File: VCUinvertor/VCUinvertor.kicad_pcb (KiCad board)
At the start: 2 copper layers, 97.3 x 113.8 mm, 107 parts, among them J7 PowerSupply, J9 BRAKE LIGHT, Q1 2N7002, Q10 2N7002, Q11 BC848C, Q12 BCP51, Q2 2N7002, Q3 2N7002, Q4 2N7002, Q5 2N7002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

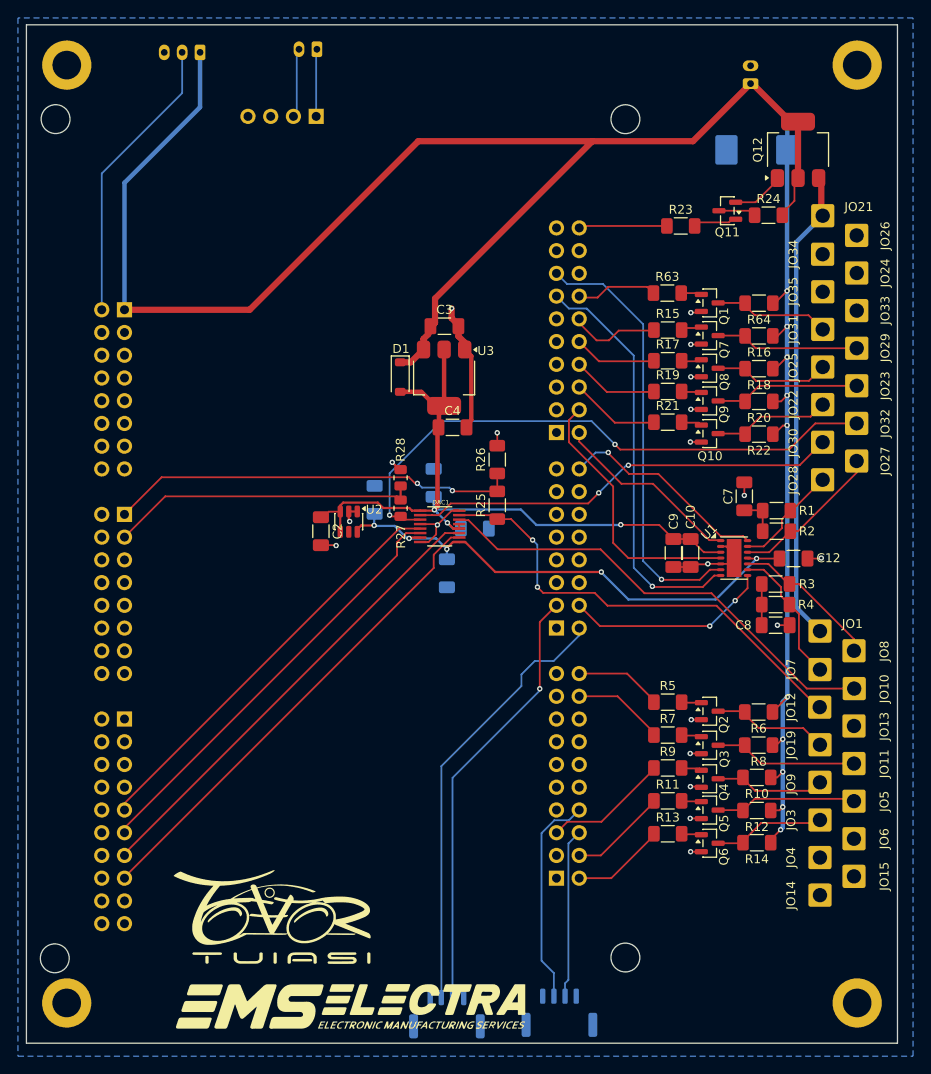
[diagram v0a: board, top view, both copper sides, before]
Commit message: TestPoints added
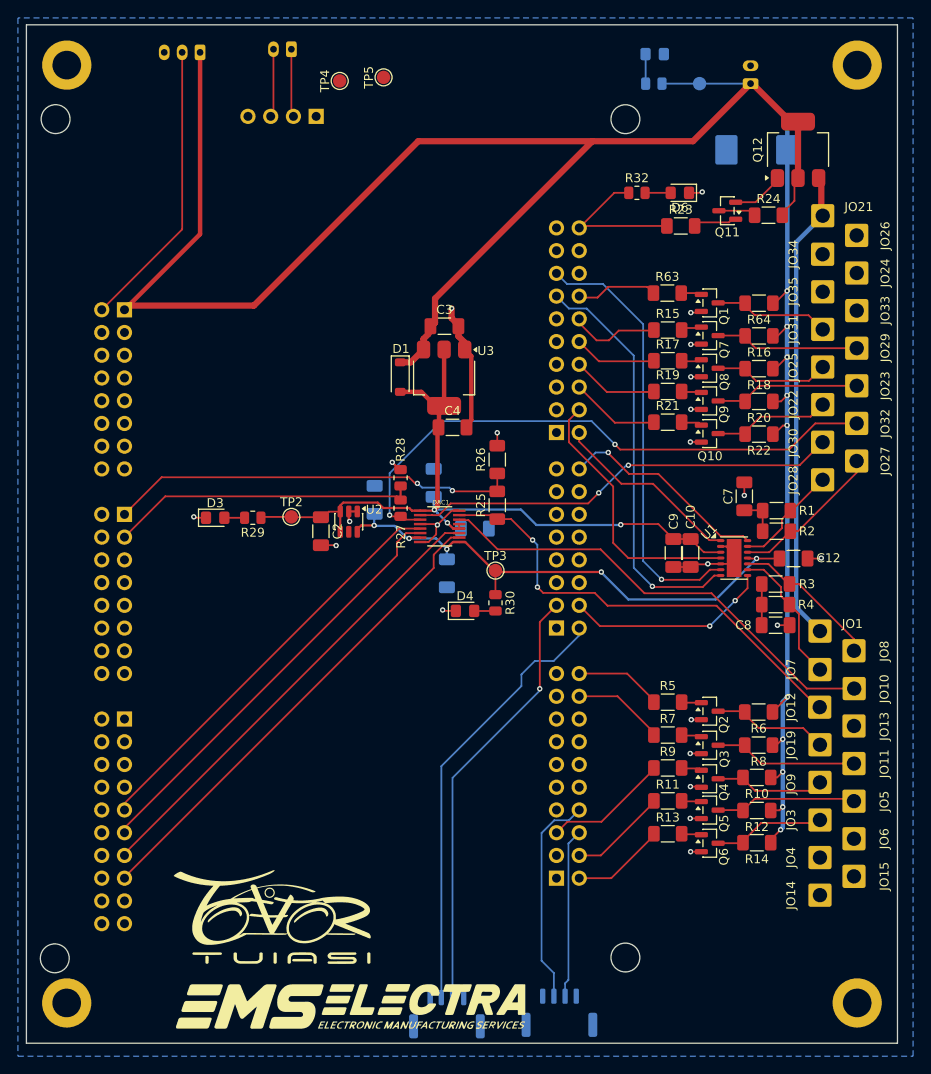
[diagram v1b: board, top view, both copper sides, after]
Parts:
- added 12V1: 12V, TestPoint:TestPoint_Pad_D1.5mm, B.Cu at (128.2, 44.3)
- added D3: LED, LED_SMD:LED_0805_2012Metric_Pad1.15x1.40mm_HandSolder, F.Cu at (74.0, 92.8)
- added D4: LED, LED_SMD:LED_0805_2012Metric_Pad1.15x1.40mm_HandSolder, F.Cu at (102.0, 103.2)
- added D5: LED, LED_SMD:LED_0805_2012Metric_Pad1.15x1.40mm_HandSolder, B.Cu at (123.1, 41.0)
- added D6: LED, LED_SMD:LED_0805_2012Metric_Pad1.15x1.40mm_HandSolder, F.Cu at (126.0, 56.5)
- added R29: 1k, Resistor_SMD:R_0805_2012Metric, F.Cu at (78.2, 92.8)
- added R30: 1k, Resistor_SMD:R_0805_2012Metric, F.Cu at (105.4, 102.3)
- added R31: 2.2k, Resistor_SMD:R_0805_2012Metric, B.Cu at (123.0, 44.3)
- added R32: 1k, Resistor_SMD:R_0805_2012Metric, F.Cu at (121.2, 56.5)
- added TP2: 5V, TestPoint:TestPoint_Pad_D1.5mm, F.Cu at (82.6, 92.7)
- added TP3: 3.3V, TestPoint:TestPoint_Pad_D1.5mm, F.Cu at (105.4, 98.7)
- added TP4: CANH, TestPoint:TestPoint_Pad_D1.5mm, F.Cu at (88.0, 44.0)
- added TP5: CANL, TestPoint:TestPoint_Pad_D1.5mm, F.Cu at (92.9, 43.6)
- moved CA1 2.85 mm to (82.6, 40.5)
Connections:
- CA0 pad 1: Net-(CA0-Pin_1) -> unconnected-(CA0-Pin_1-Pad1)
- CA0 pad 3: unconnected-(CA0-Pin_3-Pad3) -> Net-(CA0-Pin_3)
- CA1 pad 1: Net-(CA0-Pin_1) -> Net-(CA0-Pin_2)
- CA1 pad 2: Net-(CA0-Pin_2) -> Net-(CA0-Pin_3)
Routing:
- net +12V: track 270.1 -> 280.1 mm
- net Net-(CA0-Pin_3): track 0.00 -> 7.63 mm
- net Net-(CA0-Pin_1): track 7.53 -> 0.00 mm
- net INV_OFF: track 9.88 -> 17.0 mm
- net +5V: track 82.1 -> 88.9 mm
- net GND: track 56.2 -> 60.6 mm, vias 20 -> 23
- net Net-(D5-A): track 0.00 -> 3.31 mm
- net Net-(D6-A): track 0.00 -> 2.86 mm
- net +3.3V: track 58.7 -> 61.3 mm
- net Net-(D4-A): track 0.00 -> 2.38 mm
- net Net-(D3-A): track 0.00 -> 2.26 mm

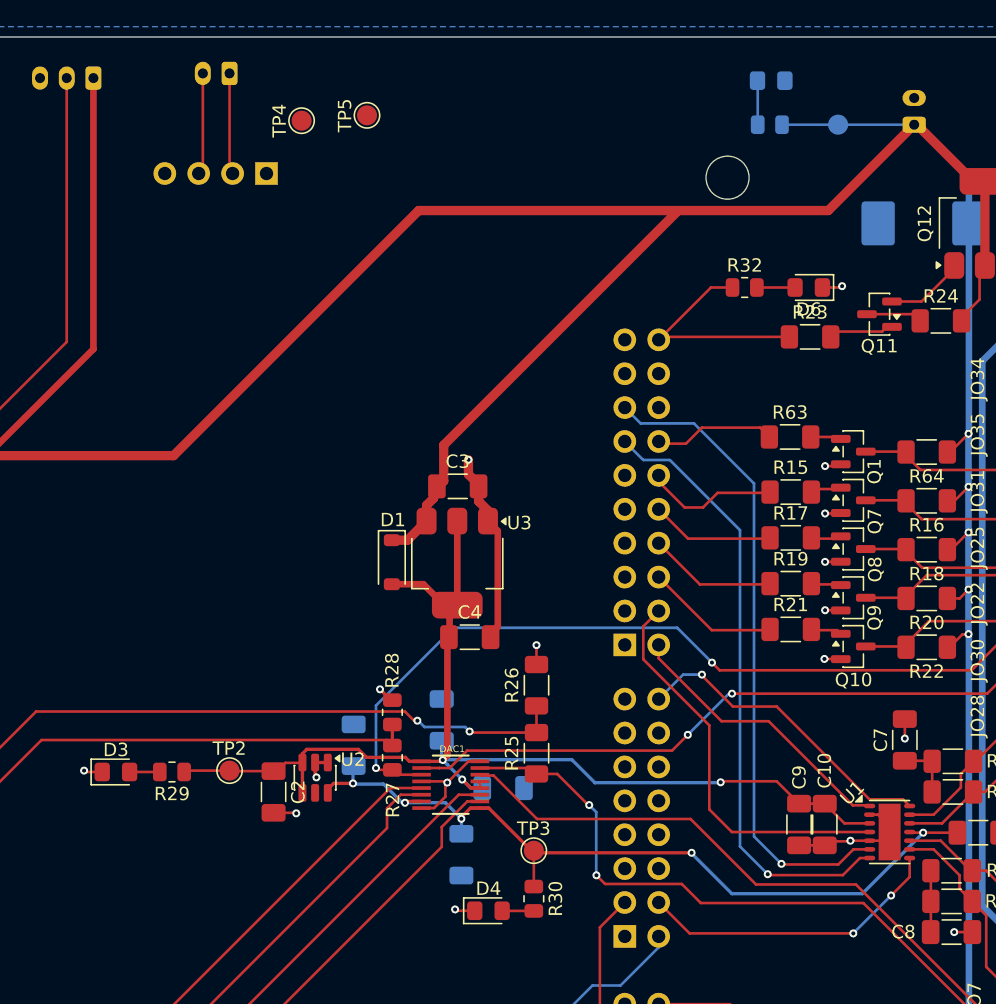
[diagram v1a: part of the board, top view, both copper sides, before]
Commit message: Ref LEDs added
For 3.3V & 5V & ...
Added for easy testing, LEDs running 2-3 mA each
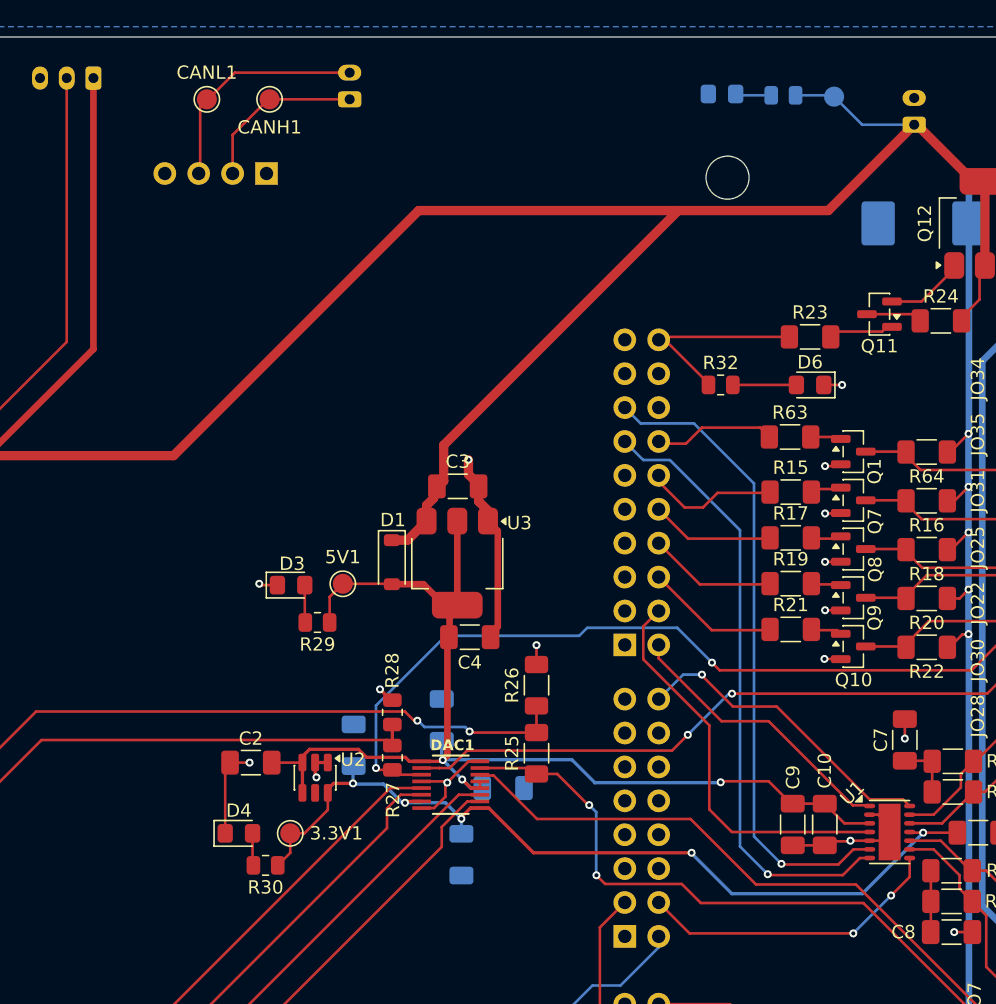
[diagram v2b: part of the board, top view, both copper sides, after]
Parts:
- moved R30 20.3 mm to (85.3, 99.8), turned to 180 degrees
- moved D4 19.6 mm to (83.3, 97.4)
- moved D3 19.2 mm to (87.2, 78.8)
- moved 3.3V1 18.3 mm to (87.1, 97.4), turned to -90 degrees
- moved 5V1 16.4 mm to (91.0, 78.7)
- moved R29 15.6 mm to (89.1, 81.6)
- moved CANL1 12.1 mm to (80.9, 42.4), turned to 180 degrees
- moved CA1 9.21 mm to (91.6, 42.4), turned to 90 degrees
- moved R32 7.52 mm to (119.4, 63.8)
- moved D6 7.30 mm to (126.1, 63.8)
- moved D5 3.82 mm to (119.5, 42.0), turned to 0 degrees
- moved CANH1 2.88 mm to (85.6, 42.4), turned to 180 degrees
- moved C2 2.78 mm to (84.2, 92.1), turned to 180 degrees
- moved R31 2.42 mm to (124.1, 42.1)
- moved 12V1 2.12 mm to (127.9, 42.2)
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- renumbered TP3 to 3.3V1, TP2 to 5V1, TP4 to CANH1, TP5 to CANL1
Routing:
- net Net-(CA0-Pin_3): track 7.63 -> 17.3 mm
- net Net-(CA0-Pin_2): track 7.60 -> 12.8 mm
- net +3.3V: track 61.3 -> 66.3 mm
- net GND: track 60.6 -> 64.7 mm, vias 23 -> 22
- net INV_OFF: track 17.0 -> 14.9 mm
- net Net-(D6-A): track 2.86 -> 4.76 mm
- net Net-(D5-A): track 3.31 -> 2.70 mm
- net Net-(D3-A): track 2.26 -> 2.82 mm
